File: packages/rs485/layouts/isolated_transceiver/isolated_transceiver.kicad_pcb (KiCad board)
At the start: 2 copper layers, 9 parts

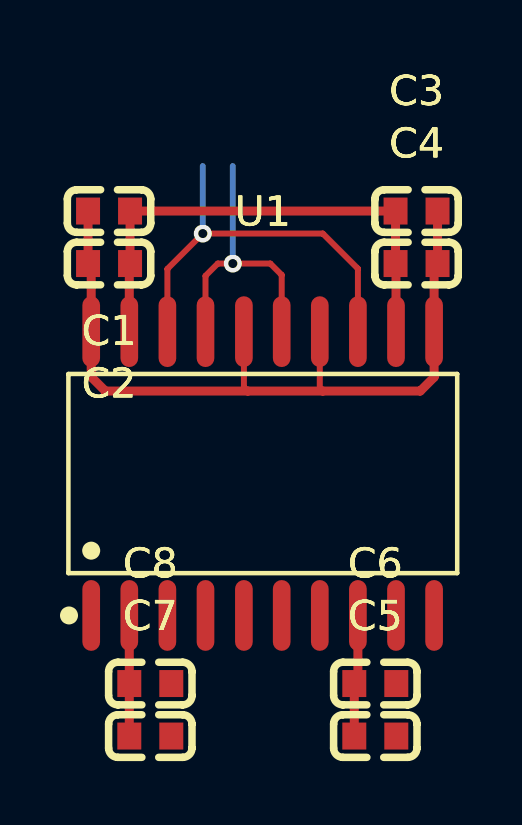
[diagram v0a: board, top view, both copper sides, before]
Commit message: Fix pulldown on RE pins
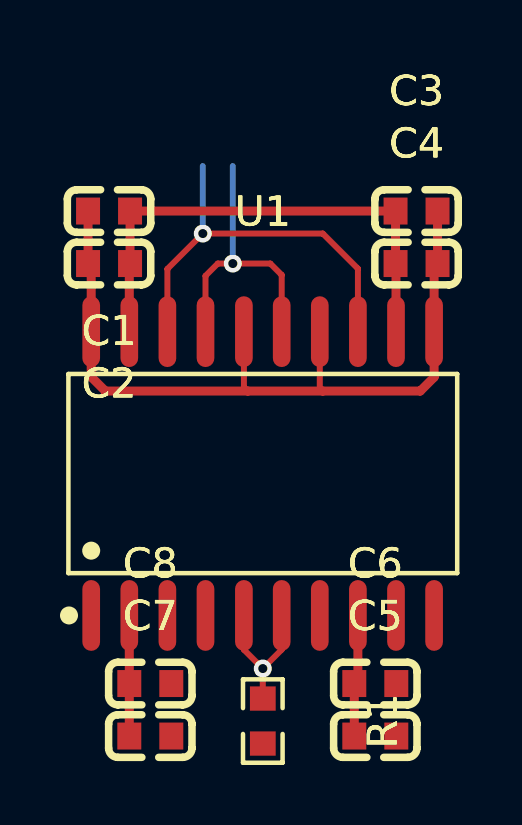
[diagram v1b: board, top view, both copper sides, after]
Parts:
- added R1: 10kΩ ±1% 100mW, atopile:R0603-ebcab9, F.Cu at (0.00, 8.25)
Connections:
- C1 pad 1: hv-1 -> hv
- C2 pad 1: hv-1 -> hv
- C3 pad 1: hv-1 -> hv
- C4 pad 1: hv-1 -> hv
- C5 pad 1: hv -> hv-1
- C6 pad 1: hv -> hv-1
- C7 pad 1: hv -> hv-1
- C8 pad 1: hv -> hv-1
- U1 pad 12: hv-1 -> hv
- U1 pad 13: transceiver-line -> transceiver-line-1
- U1 pad 15: transceiver-line-2 -> transceiver-line
- U1 pad 17: transceiver-line-2 -> transceiver-line
- U1 pad 18: transceiver-line -> transceiver-line-1
- U1 pad 19: hv-1 -> hv
- U1 pad 2: hv -> hv-1
- U1 pad 4: transceiver-line-5 -> transceiver-line-2
- U1 pad 5: transceiver-line-4 -> line
- U1 pad 6: transceiver-line-3 -> line
- U1 pad 7: transceiver-line-1 -> transceiver-line-3
- U1 pad 8: hv -> hv-1
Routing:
- net transceiver-line-1: track 0.00 -> 13.8 mm, vias 0 -> 1
- net transceiver-line-2: track 9.87 -> 0.00 mm, vias 1 -> 0
- net hv-1: track 16.9 -> 8.09 mm
- net hv: track 8.09 -> 16.9 mm
- net line: track 0.00 -> 5.06 mm, vias 0 -> 1
- net transceiver-line: track 13.8 -> 9.87 mm

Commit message: Build all packages without designators on silkscreen.
Also disable fail_on_drc and enable keep_picked_parts for build
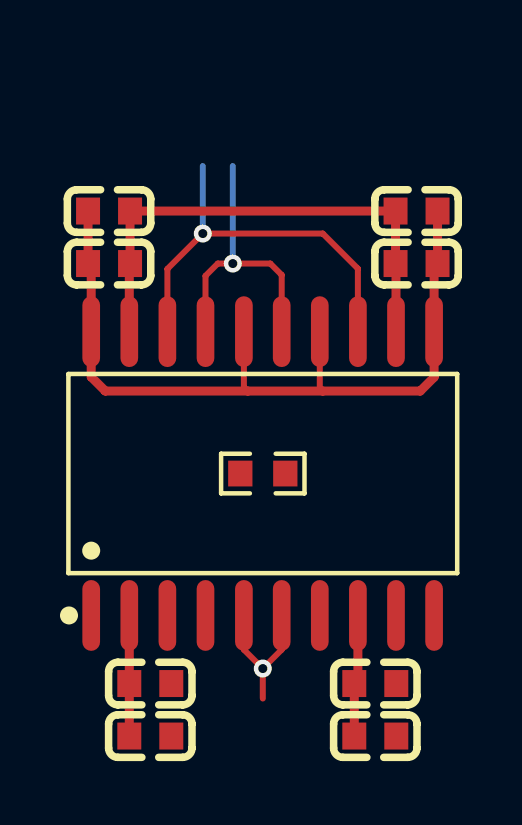
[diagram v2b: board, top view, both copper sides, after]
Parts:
- moved R1 8.25 mm to (0.00, 0.00), turned to 0 degrees
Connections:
- C1 pad 1: hv -> hv-1
- C2 pad 1: hv -> hv-1
- C3 pad 1: hv -> hv-1
- C4 pad 1: hv -> hv-1
- C5 pad 1: hv-1 -> hv
- C6 pad 1: hv-1 -> hv
- C7 pad 1: hv-1 -> hv
- C8 pad 1: hv-1 -> hv
- U1 pad 12: hv -> hv-1
- U1 pad 13: transceiver-line-1 -> transceiver-line
- U1 pad 15: transceiver-line -> transceiver-line-1
- U1 pad 17: transceiver-line -> transceiver-line-1
- U1 pad 18: transceiver-line-1 -> transceiver-line
- U1 pad 19: hv -> hv-1
- U1 pad 2: hv-1 -> hv
- U1 pad 8: hv-1 -> hv
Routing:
- net hv-1: track 8.09 -> 16.9 mm
- net hv: track 16.9 -> 8.09 mm
- net line: track 5.06 -> 0.00 mm, vias 1 -> 0
- net (no net): track 0.00 -> 5.06 mm, vias 0 -> 1
- net transceiver-line-1: track 13.8 -> 9.87 mm
- net transceiver-line: track 9.87 -> 13.8 mm

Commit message: Fix publish on failed build & fix pull resistor that should not be there (#2)
* Remove pull resistor (should not be part of the tranceiver)

* Fix publish if build fails
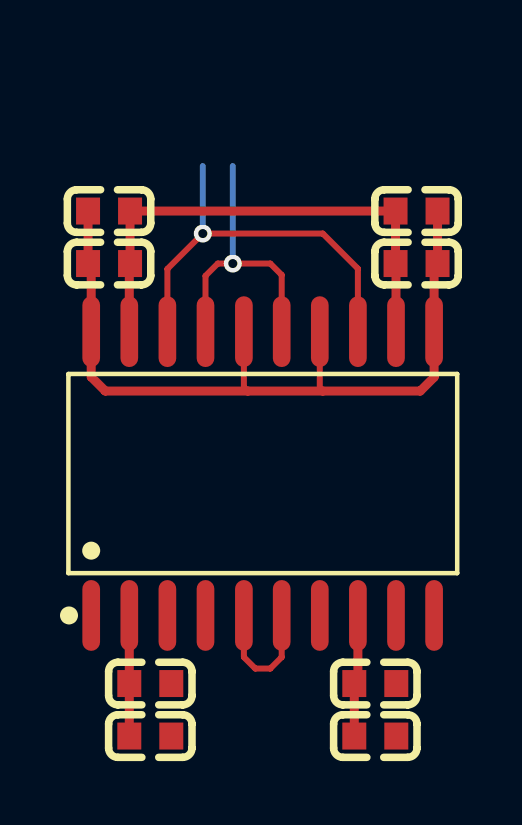
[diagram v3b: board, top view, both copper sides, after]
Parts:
- removed R1: 10kΩ ±1% 100mW, atopile:R0603-ebcab9
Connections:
- net line renamed transceiver-line-4
- U1 pad 13: transceiver-line -> transceiver-line-1
- U1 pad 15: transceiver-line-1 -> transceiver-line-3
- U1 pad 17: transceiver-line-1 -> transceiver-line-3
- U1 pad 18: transceiver-line -> transceiver-line-1
- U1 pad 4: transceiver-line-2 -> transceiver-line
- U1 pad 7: transceiver-line-3 -> transceiver-line-2
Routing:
- net transceiver-line: track 13.8 -> 0.00 mm, vias 1 -> 0
- net transceiver-line-3: track 0.00 -> 9.87 mm, vias 0 -> 1
- net (no net): track 5.06 -> 0.00 mm, vias 1 -> 0
- net transceiver-line-4: track 0.00 -> 4.35 mm
- net transceiver-line-1: track 9.87 -> 13.8 mm

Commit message: Rebuild rs485 package
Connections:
- C1 pad 2: gnd-1 -> gnd
- C2 pad 2: gnd-1 -> gnd
- C3 pad 2: gnd-1 -> gnd
- C4 pad 2: gnd-1 -> gnd
- C5 pad 2: gnd -> gnd-1
- C6 pad 2: gnd -> gnd-1
- C7 pad 2: gnd -> gnd-1
- C8 pad 2: gnd -> gnd-1
- U1 pad 1: gnd -> gnd-1
- U1 pad 10: gnd -> gnd-1
- U1 pad 11: gnd-1 -> gnd
- U1 pad 13: transceiver-line-1 -> transceiver-line-4
- U1 pad 14: gnd-1 -> gnd
- U1 pad 15: transceiver-line-3 -> transceiver-line-1
- U1 pad 16: gnd-1 -> gnd
- U1 pad 17: transceiver-line-3 -> transceiver-line-1
- U1 pad 18: transceiver-line-1 -> transceiver-line-4
- U1 pad 20: gnd-1 -> gnd
- U1 pad 3: gnd -> gnd-1
- U1 pad 4: transceiver-line -> transceiver-line-3
- U1 pad 5: transceiver-line-4 -> transceiver-line-2
- U1 pad 6: transceiver-line-4 -> transceiver-line-2
- U1 pad 7: transceiver-line-2 -> transceiver-line
- U1 pad 9: gnd -> gnd-1
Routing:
- net gnd-1: track 27.0 -> 0.00 mm
- net gnd: track 0.00 -> 27.0 mm
- net transceiver-line-3: track 9.87 -> 0.00 mm, vias 1 -> 0
- net transceiver-line-4: track 4.35 -> 13.8 mm, vias 0 -> 1
- net transceiver-line-2: track 0.00 -> 4.35 mm
- net transceiver-line-1: track 13.8 -> 9.87 mm
